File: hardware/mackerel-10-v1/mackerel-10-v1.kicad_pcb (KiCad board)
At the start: 2 copper layers, 160 x 100 mm, 14 parts, among them J1 Conn_02x05_Odd_Even, U1 68010D, U2 AS6C4008-55PCN, U3 SST39SF040, U4 AS6C4008-55PCN, U5 SST39SF040, U6 XR68C681, X1 40 MHz, X2 3.6864 MHz

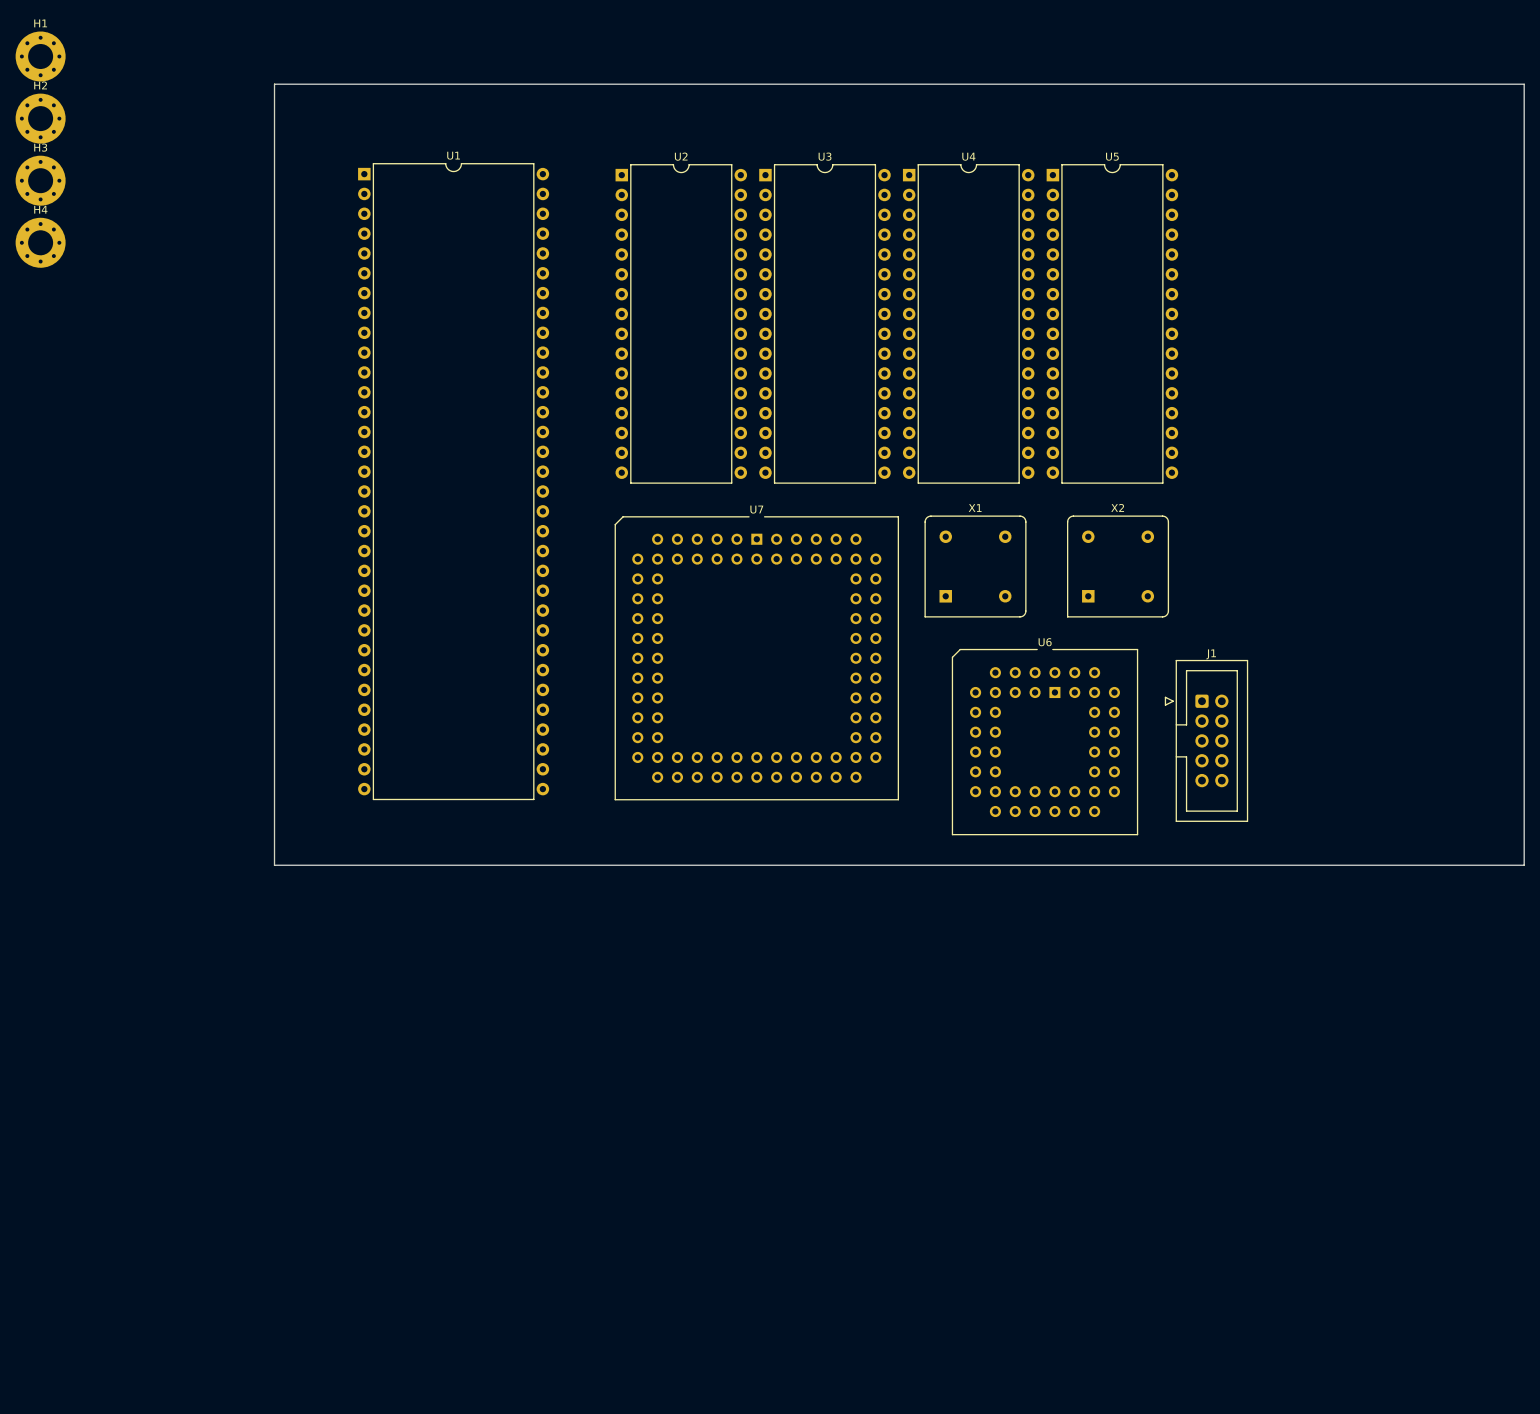
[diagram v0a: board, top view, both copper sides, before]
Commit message: Symbol and footprint for SIMM-30 DRAM stubbed out
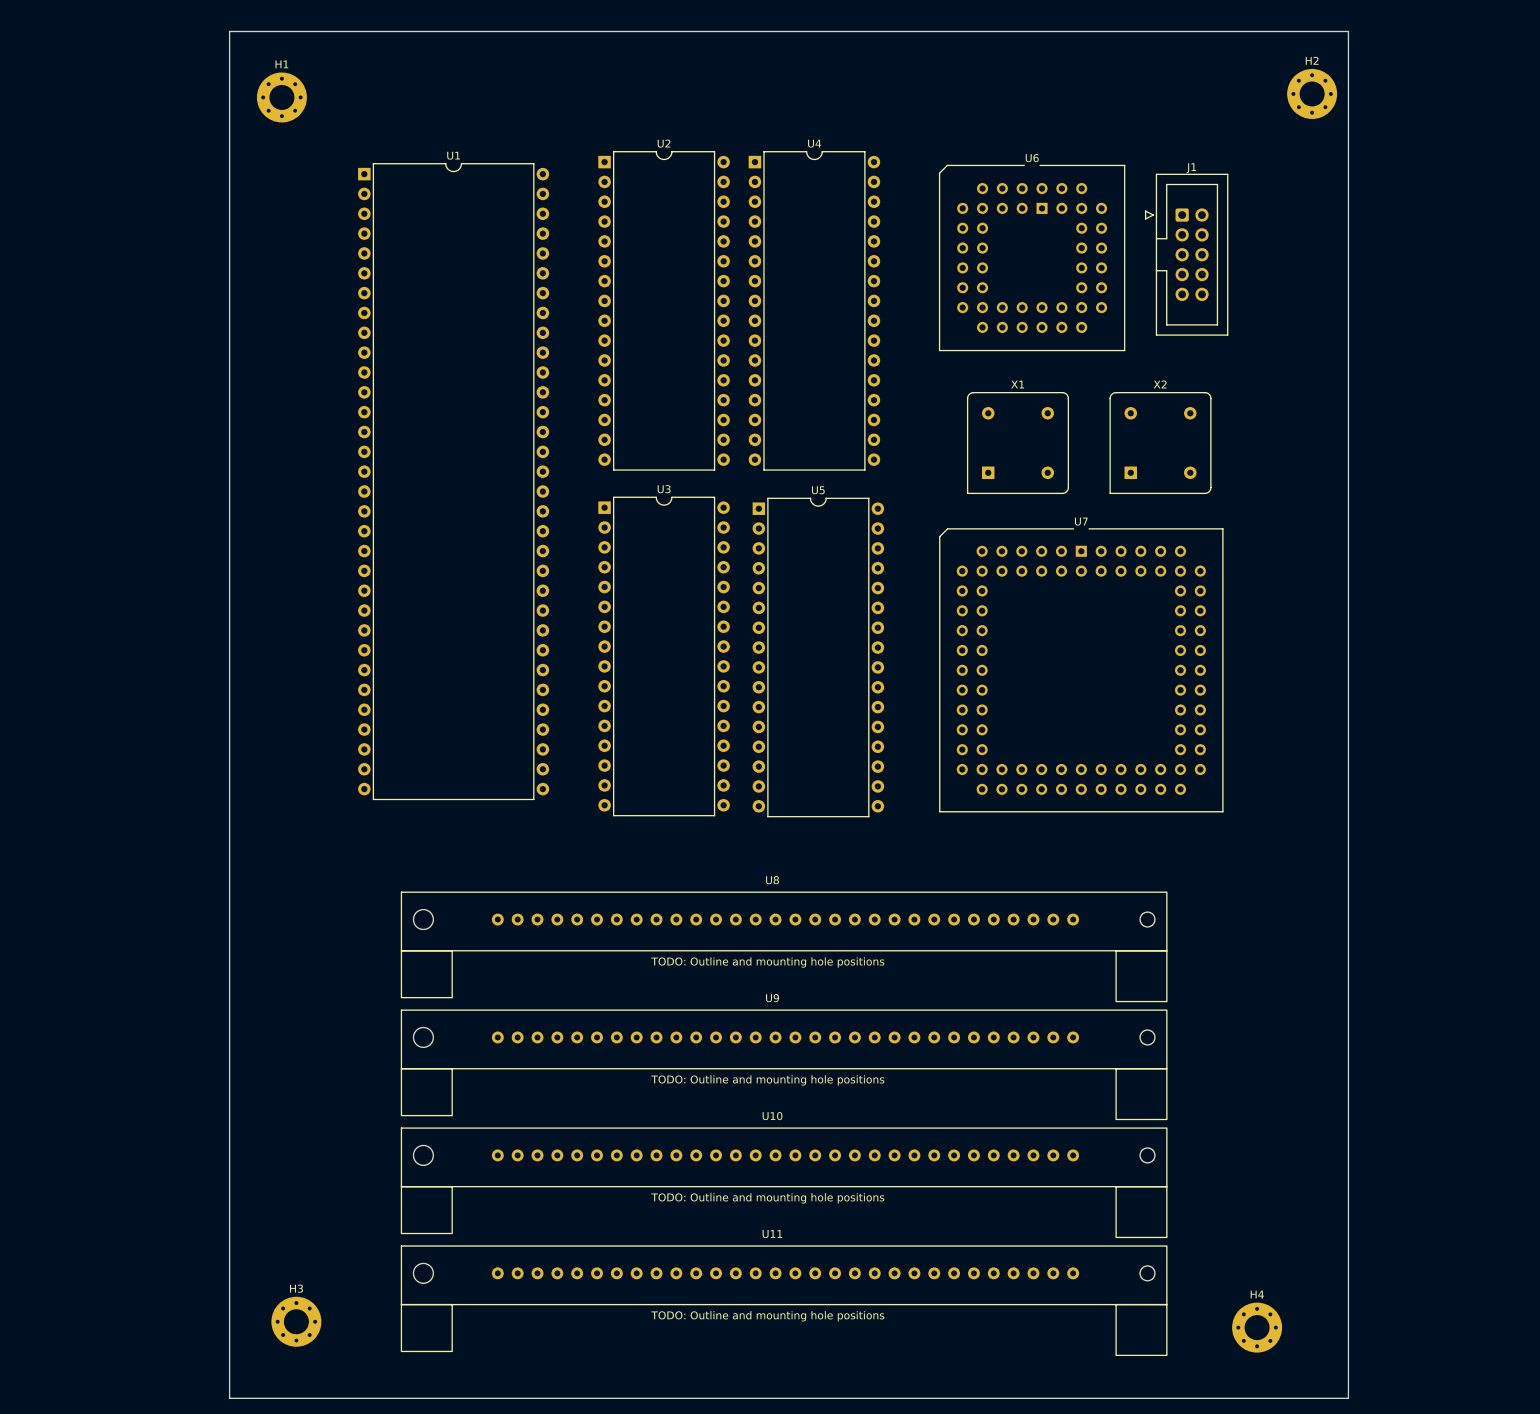
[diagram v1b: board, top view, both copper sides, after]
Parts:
- added U10: ~, mackerel:SIMM-30, F.Cu at (122.2, 157.2)
- added U11: ~, mackerel:SIMM-30, F.Cu at (122.2, 172.2)
- added U8: ~, mackerel:SIMM-30, F.Cu at (122.2, 127.0)
- added U9: ~, mackerel:SIMM-30, F.Cu at (122.2, 142.1)
- moved H4 208.7 mm to (145.8, 179.2)
- moved H2 162.8 mm to (152.8, 21.2)
- moved H3 149.7 mm to (22.8, 178.4)
- moved J1 62.3 mm to (136.2, 36.8)
- moved U6 62.0 mm to (118.3, 35.9)
- moved U5 56.9 mm to (82.0, 74.3)
- moved U3 47.3 mm to (62.3, 74.2)
- moved U7 41.6 mm to (123.3, 79.8)
- moved H1 31.3 mm to (20.9, 21.7)
- moved U4 19.8 mm to (81.5, 30.0)
- moved X1 16.7 mm to (111.4, 69.8)
- moved X2 16.7 mm to (129.6, 69.8)
- moved U2 2.76 mm to (62.3, 30.0)
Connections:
- net /CLK_SYS renamed /CLK_SRC
- U1 pad 15: unconnected-(U1-CLK-Pad15) -> CLK_CPU
- U1 pad 21: unconnected-(U1-VPA-Pad21) -> /VPA
- U7 pad 10: unconnected-(U7-IO-Pad10) -> IPL2
- U7 pad 12: unconnected-(U7-IO-Pad12) -> FC0
- U7 pad 15: unconnected-(U7-IO-Pad15) -> FC1
- U7 pad 16: unconnected-(U7-IO-Pad16) -> FC2
- U7 pad 28: unconnected-(U7-IO-Pad28) -> /VPA
- U7 pad 29: unconnected-(U7-IO-Pad29) -> /BERR
- U7 pad 31: unconnected-(U7-IO-Pad31) -> /DTACK
- U7 pad 33: unconnected-(U7-IO-Pad33) -> A1
- U7 pad 34: unconnected-(U7-IO-Pad34) -> A2
- U7 pad 35: unconnected-(U7-IO-Pad35) -> A3
- U7 pad 36: unconnected-(U7-IO-Pad36) -> A4
- U7 pad 37: unconnected-(U7-IO-Pad37) -> A5
- U7 pad 39: unconnected-(U7-IO-Pad39) -> A6
- U7 pad 4: unconnected-(U7-IO-Pad4) -> CLK_CPU
- U7 pad 40: unconnected-(U7-IO-Pad40) -> A7
- U7 pad 41: unconnected-(U7-IO-Pad41) -> A8
- U7 pad 44: unconnected-(U7-IO-Pad44) -> A9
- U7 pad 45: unconnected-(U7-IO-Pad45) -> A10
- U7 pad 46: unconnected-(U7-IO-Pad46) -> A11
- U7 pad 48: unconnected-(U7-IO-Pad48) -> A12
- U7 pad 49: unconnected-(U7-IO-Pad49) -> A13
- U7 pad 50: unconnected-(U7-IO-Pad50) -> A14
- U7 pad 51: unconnected-(U7-IO-Pad51) -> A15
- U7 pad 52: unconnected-(U7-IO-Pad52) -> A16
- U7 pad 54: unconnected-(U7-IO-Pad54) -> A17
- U7 pad 55: unconnected-(U7-IO-Pad55) -> A18
- U7 pad 56: unconnected-(U7-IO-Pad56) -> A19
- U7 pad 57: unconnected-(U7-IO-Pad57) -> A20
- U7 pad 58: unconnected-(U7-IO-Pad58) -> A21
- U7 pad 60: unconnected-(U7-IO-Pad60) -> A22
- U7 pad 61: unconnected-(U7-IO-Pad61) -> A23
- U7 pad 64: unconnected-(U7-IO-Pad64) -> /AS
- U7 pad 65: unconnected-(U7-IO-Pad65) -> /UDS
- U7 pad 67: unconnected-(U7-IO-Pad67) -> /LDS
- U7 pad 68: unconnected-(U7-IO-Pad68) -> R/W
- U7 pad 73: unconnected-(U7-IO-Pad73) -> D0
- U7 pad 74: unconnected-(U7-IO-Pad74) -> D1
- U7 pad 75: unconnected-(U7-IO-Pad75) -> D2
- U7 pad 76: unconnected-(U7-IO-Pad76) -> D3
- U7 pad 77: unconnected-(U7-IO-Pad77) -> D4
- U7 pad 79: unconnected-(U7-IO-Pad79) -> D5
- U7 pad 8: unconnected-(U7-IO-Pad8) -> IPL0
- U7 pad 80: unconnected-(U7-IO-Pad80) -> D6
- U7 pad 81: unconnected-(U7-IO-Pad81) -> D7
- U7 pad 9: unconnected-(U7-IO-Pad9) -> IPL1
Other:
- board size 160 x 100 mm -> 143.2 x 175 mm

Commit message: Trying to figure out Mackerel-10 components
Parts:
- removed H1, H2, H3, H4: MountingHole_Pad, MountingHole:MountingHole_3.2mm_M3_Pad_Via
- removed U10, U11: ~, mackerel:SIMM-30
- removed the U2 at (62.3, 30.0)
- added C1: C_Polarized, Capacitor_THT:CP_Radial_D5.0mm_P2.50mm, F.Cu at (-20.6, -14.1)
- added C2: C_Polarized, Capacitor_THT:CP_Radial_D10.0mm_P5.00mm, F.Cu at (44.0, 28.5)
- added C3: C_Polarized, Capacitor_THT:CP_Radial_D10.0mm_P5.00mm, F.Cu at (-46.0, -16.8)
- added D1: LED, LED_THT:LED_D5.0mm, F.Cu at (-35.3, -13.6)
- added D2: LED, LED_THT:LED_D5.0mm, F.Cu at (-27.8, -13.6)
- added J2: DIN41612_02x32_AC, Connector_DIN:DIN41612_C_2x32_Male_Horizontal_THT, F.Cu at (175.0, 30.4)
- added J3: DE9_Plug_MountingHoles, Connector_Dsub:DSUB-9_Male_Horizontal_P2.77x2.84mm_EdgePinOffset7.70mm_Housed_MountingHolesOffset9.12mm, F.Cu at (30.8, 47.0)
- added J4: Conn_01x06, Connector_PinSocket_2.54mm:PinSocket_1x06_P2.54mm_Horizontal, F.Cu at (-168.4, 65.6)
- added J5: Conn_01x06, Connector_PinSocket_2.54mm:PinSocket_1x06_P2.54mm_Horizontal, F.Cu at (-167.9, 44.2)
- added J6: DC_Jack, Connector_BarrelJack:BarrelJack_GCT_DCJ200-10-A_Horizontal, F.Cu at (34.5, 25.2)
- added J7: DE9_Plug_MountingHoles, Connector_Dsub:DSUB-9_Male_Horizontal_P2.77x2.84mm_EdgePinOffset7.70mm_Housed_MountingHolesOffset9.12mm, F.Cu at (30.8, 82.0)
- added JP1: Jumper_2_Open, Connector_PinHeader_2.54mm:PinHeader_1x02_P2.54mm_Vertical, F.Cu at (-34.3, 50.0)
- added JP2: Jumper_2_Open, Connector_PinHeader_2.54mm:PinHeader_1x02_P2.54mm_Vertical, F.Cu at (-29.6, 50.0)
- added R1: R, Resistor_THT:R_Axial_DIN0204_L3.6mm_D1.6mm_P5.08mm_Horizontal, F.Cu at (-22.7, 80.7)
- added R10: R, Resistor_THT:R_Axial_DIN0207_L6.3mm_D2.5mm_P7.62mm_Horizontal, F.Cu at (-23.8, -32.1)
- added R11: R, Resistor_THT:R_Axial_DIN0207_L6.3mm_D2.5mm_P7.62mm_Horizontal, F.Cu at (-23.8, -28.1)
- added R12: R, Resistor_THT:R_Axial_DIN0207_L6.3mm_D2.5mm_P7.62mm_Horizontal, F.Cu at (-23.8, -24.0)
- added R13: R, Resistor_THT:R_Axial_DIN0207_L6.3mm_D2.5mm_P7.62mm_Horizontal, F.Cu at (-23.8, -19.9)
- added R2: R, Resistor_THT:R_Axial_DIN0204_L3.6mm_D1.6mm_P5.08mm_Horizontal, F.Cu at (-22.7, 83.8)
- added R3: R, Resistor_THT:R_Axial_DIN0204_L3.6mm_D1.6mm_P5.08mm_Horizontal, F.Cu at (-22.7, 87.0)
- added R4: R, Resistor_THT:R_Axial_DIN0204_L3.6mm_D1.6mm_P5.08mm_Horizontal, F.Cu at (-22.7, 90.1)
- added R5: R, Resistor_THT:R_Axial_DIN0204_L3.6mm_D1.6mm_P5.08mm_Horizontal, F.Cu at (-22.7, 93.3)
- added R6: R, Resistor_THT:R_Axial_DIN0204_L3.6mm_D1.6mm_P5.08mm_Horizontal, F.Cu at (19.6, 180.2)
- added R7: R, Resistor_THT:R_Axial_DIN0204_L3.6mm_D1.6mm_P5.08mm_Horizontal, F.Cu at (19.6, 183.3)
- added R8: R, Resistor_THT:R_Axial_DIN0204_L3.6mm_D1.6mm_P5.08mm_Horizontal, F.Cu at (19.6, 186.5)
- added R9: R, Resistor_THT:R_Axial_DIN0204_L3.6mm_D1.6mm_P5.08mm_Horizontal, F.Cu at (19.6, 177.1)
- added SW1: SW_Push, Button_Switch_THT:SW_PUSH_6mm_H5mm, F.Cu at (-21.7, -7.80)
- added U12: NE555P, Package_DIP:DIP-8_W7.62mm, F.Cu at (-47.9, -8.95)
- added U6: KM62256CLP, Package_DIP:DIP-28_W15.24mm, F.Cu at (81.4, -32.2)
- U4: value AS6C4008-55PCN -> KM62256CLP; footprint Package_DIP:DIP-32_W15.24mm -> Package_DIP:DIP-28_W15.24mm
- U8, U9: value ~ -> MAX3232; footprint mackerel:SIMM-30 -> Package_DIP:DIP-16_W7.62mm
- X1: value 40 MHz -> 50 MHz
- moved X2 356.0 mm to (-180.8, -104.4)
- moved X1 331.3 mm to (-180.2, -87.5)
- moved U7 225.3 mm to (-103.5, 75.8)
- moved J1 170.9 mm to (19.4, 161.5), turned to 90 degrees
- moved U5 114.9 mm to (125.4, -32.0), turned to 90 degrees
- moved U9 110.3 mm to (45.4, 62.9), turned to 90 degrees
- moved U8 108.8 mm to (45.2, 50.1), turned to 90 degrees
- moved U3 107.1 mm to (125.1, -12.6), turned to 90 degrees
- moved U2 62.5 mm to (61.0, 74.5)
- moved U1 50.4 mm to (79.5, 47.2), turned to 90 degrees
- moved U4 41.7 mm to (81.5, -11.8), turned to 90 degrees
- renumbered U7 to U2, U6 to U7
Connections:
- U1 pad 12: unconnected-(U1-BGACK-Pad12) -> Net-(U1-BGACK)
- U1 pad 13: unconnected-(U1-BR-Pad13) -> Net-(U1-BR)
- U1 pad 17: unconnected-(U1-HALT-Pad17) -> /RESET
- U1 pad 18: unconnected-(U1-RESET-Pad18) -> /RESET
- U2 pad 10: IPL2 -> /ODDROM
- U2 pad 11: unconnected-(U7-IO-Pad11) -> /DUART
- U2 pad 12: FC0 -> /EXP
- U2 pad 15: FC1 -> /DTACK_DUART
- U2 pad 16: FC2 -> /DTACK_EXP
- U2 pad 17: unconnected-(U7-IO-Pad17) -> /IRQ1
- U2 pad 18: unconnected-(U7-IO-Pad18) -> /IRQ2
- U2 pad 2: GND -> unconnected-(U2-OE2/GCLK2-Pad2)
- U2 pad 20: unconnected-(U7-IO-Pad20) -> /IRQ3
- U2 pad 21: unconnected-(U7-IO-Pad21) -> /IACK1
- U2 pad 22: unconnected-(U7-IO-Pad22) -> /IACK2
- U2 pad 24: unconnected-(U7-IO-Pad24) -> /IACK3
- U2 pad 25: unconnected-(U7-IO-Pad25) -> FC0
- U2 pad 27: unconnected-(U7-IO-Pad27) -> FC1
- U2 pad 28: /VPA -> FC2
- U2 pad 29: /BERR -> /VPA
- U2 pad 30: unconnected-(U7-IO-Pad30) -> /BERR
- U2 pad 33: A1 -> A16
- U2 pad 34: A2 -> A17
- U2 pad 35: A3 -> A18
- U2 pad 36: A4 -> A19
- U2 pad 37: A5 -> A20
- U2 pad 39: A6 -> A21
- U2 pad 40: A7 -> A22
- U2 pad 41: A8 -> A23
- U2 pad 44: A9 -> unconnected-(U2-IO-Pad44)
- U2 pad 45: A10 -> unconnected-(U2-IO-Pad45)
- U2 pad 46: A11 -> unconnected-(U2-IO-Pad46)
- U2 pad 48: A12 -> unconnected-(U2-IO-Pad48)
- U2 pad 49: A13 -> unconnected-(U2-IO-Pad49)
- U2 pad 5: unconnected-(U7-IO-Pad5) -> /RESET
- U2 pad 50: A14 -> unconnected-(U2-IO-Pad50)
- U2 pad 51: A15 -> unconnected-(U2-IO-Pad51)
- U2 pad 52: A16 -> unconnected-(U2-IO-Pad52)
- U2 pad 54: A17 -> unconnected-(U2-IO-Pad54)
- U2 pad 55: A18 -> unconnected-(U2-IO-Pad55)
- U2 pad 56: A19 -> unconnected-(U2-IO-Pad56)
- U2 pad 57: A20 -> unconnected-(U2-IO-Pad57)
- U2 pad 58: A21 -> unconnected-(U2-IO-Pad58)
- U2 pad 6: unconnected-(U7-IO-Pad6) -> /EVENRAM
- U2 pad 60: A22 -> unconnected-(U2-IO-Pad60)
- U2 pad 61: A23 -> unconnected-(U2-IO-Pad61)
- U2 pad 64: /AS -> unconnected-(U2-IO-Pad64)
- U2 pad 65: /UDS -> unconnected-(U2-IO-Pad65)
- U2 pad 67: /LDS -> unconnected-(U2-IO-Pad67)
- U2 pad 68: R/W -> unconnected-(U2-IO-Pad68)
- U2 pad 73: D0 -> unconnected-(U2-IO-Pad73)
- U2 pad 74: D1 -> /AS
- U2 pad 75: D2 -> /UDS
- U2 pad 76: D3 -> /LDS
- U2 pad 77: D4 -> R/W
- U2 pad 79: D5 -> /IPL0
- U2 pad 8: IPL0 -> /ODDRAM
- U2 pad 80: D6 -> /IPL1
- U2 pad 81: D7 -> /IPL2
- U2 pad 9: IPL1 -> /EVENROM
- U4 pad 1: A19 -> A15
- U4 pad 10: A3 -> A1
- U4 pad 11: A2 -> D8
- U4 pad 12: A1 -> D9
- U4 pad 13: D0 -> D10
- U4 pad 14: D1 -> GND
- U4 pad 15: D2 -> D11
- U4 pad 16: GND -> D12
- U4 pad 17: D3 -> D13
- U4 pad 18: D4 -> D14
- U4 pad 19: D5 -> D15
- U4 pad 2: A17 -> A13
- U4 pad 20: D6 -> unconnected-(U4-~{CS}-Pad20)
- U4 pad 21: D7 -> A11
- U4 pad 23: A11 -> A12
- U4 pad 24: unconnected-(U4-OE#-Pad24) -> A10
- U4 pad 25: A12 -> A9
- U4 pad 26: A10 -> A14
- U4 pad 27: A9 -> unconnected-(U4-~{WE}-Pad27)
- U4 pad 28: A14 -> +5V
- U4 pad 3: A15 -> A8
- U4 pad 4: A13 -> A7
- U4 pad 5: A8 -> A6
- U4 pad 6: A7 -> A5
- U4 pad 7: A6 -> A4
- U4 pad 8: A5 -> A3
- U4 pad 9: A4 -> A2
- U8 pad 1: +5V -> unconnected-(U8-C1+-Pad1)
- U8 pad 10: D2 -> unconnected-(U8-T2IN-Pad10)
- U8 pad 11: DRAM_A4 -> unconnected-(U8-T1IN-Pad11)
- U8 pad 12: DRAM_A5 -> unconnected-(U8-R1OUT-Pad12)
- U8 pad 13: D3 -> unconnected-(U8-R1IN-Pad13)
- U8 pad 14: DRAM_A6 -> unconnected-(U8-T1OUT-Pad14)
- U8 pad 15: DRAM_A7 -> unconnected-(U8-GND-Pad15)
- U8 pad 16: D4 -> unconnected-(U8-VCC-Pad16)
- U8 pad 2: /DRAM_CAS0 -> unconnected-(U8-VS+-Pad2)
- U8 pad 3: D0 -> unconnected-(U8-C1--Pad3)
- U8 pad 4: DRAM_A0 -> unconnected-(U8-C2+-Pad4)
- U8 pad 5: DRAM_A1 -> unconnected-(U8-C2--Pad5)
- U8 pad 6: D1 -> unconnected-(U8-VS--Pad6)
- U8 pad 7: DRAM_A2 -> unconnected-(U8-T2OUT-Pad7)
- U8 pad 8: DRAM_A3 -> unconnected-(U8-R2IN-Pad8)
- U8 pad 9: GND -> unconnected-(U8-R2OUT-Pad9)
- U9 pad 1: +5V -> unconnected-(U9-C1+-Pad1)
- U9 pad 10: D10 -> unconnected-(U9-T2IN-Pad10)
- U9 pad 11: DRAM_A4 -> unconnected-(U9-T1IN-Pad11)
- U9 pad 12: DRAM_A5 -> unconnected-(U9-R1OUT-Pad12)
- U9 pad 13: D11 -> unconnected-(U9-R1IN-Pad13)
- U9 pad 14: DRAM_A6 -> unconnected-(U9-T1OUT-Pad14)
- U9 pad 15: DRAM_A7 -> unconnected-(U9-GND-Pad15)
- U9 pad 16: D12 -> unconnected-(U9-VCC-Pad16)
- U9 pad 2: /DRAM_CAS1 -> unconnected-(U9-VS+-Pad2)
- U9 pad 3: D8 -> unconnected-(U9-C1--Pad3)
- U9 pad 4: DRAM_A0 -> unconnected-(U9-C2+-Pad4)
- U9 pad 5: DRAM_A1 -> unconnected-(U9-C2--Pad5)
- U9 pad 6: D9 -> unconnected-(U9-VS--Pad6)
- U9 pad 7: DRAM_A2 -> unconnected-(U9-T2OUT-Pad7)
- U9 pad 8: DRAM_A3 -> unconnected-(U9-R2IN-Pad8)
- U9 pad 9: GND -> unconnected-(U9-R2OUT-Pad9)
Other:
- board size 143.2 x 175 mm -> 160 x 100 mm
